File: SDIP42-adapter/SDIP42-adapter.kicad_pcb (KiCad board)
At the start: 2 copper layers, 17.4 x 37.8 mm, 2 parts, among them U1 KM23C32000AG-adaptor, U2 27C322

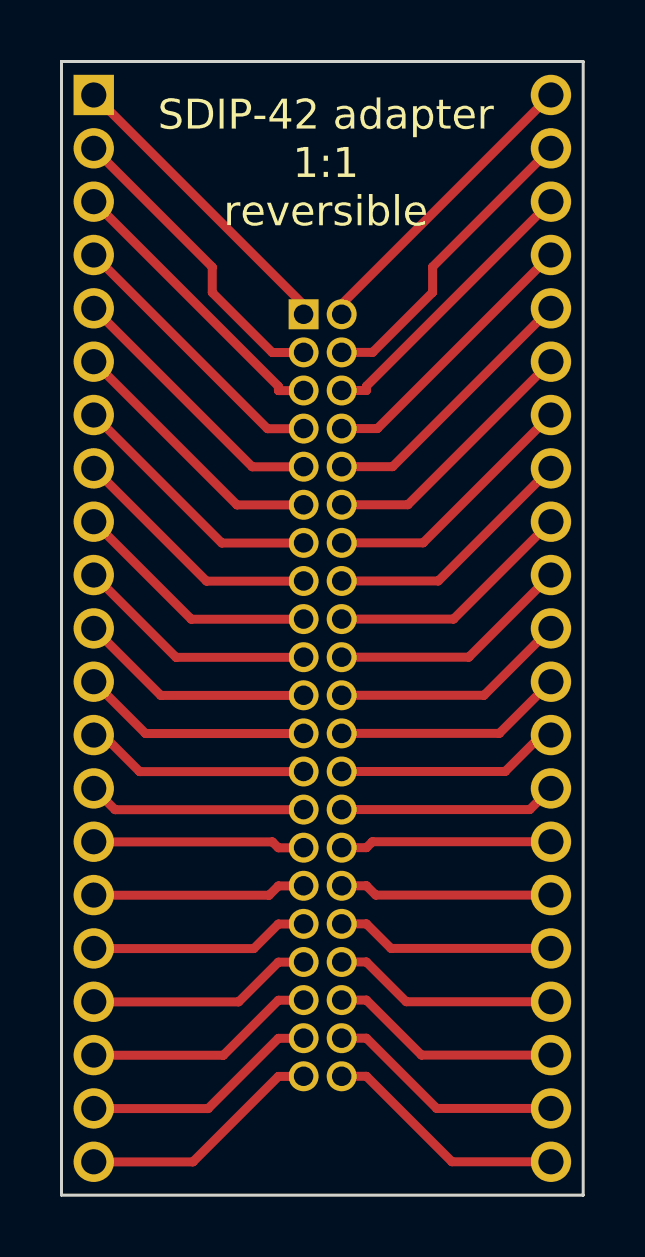
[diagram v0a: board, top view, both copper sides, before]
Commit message: rename projects, update design
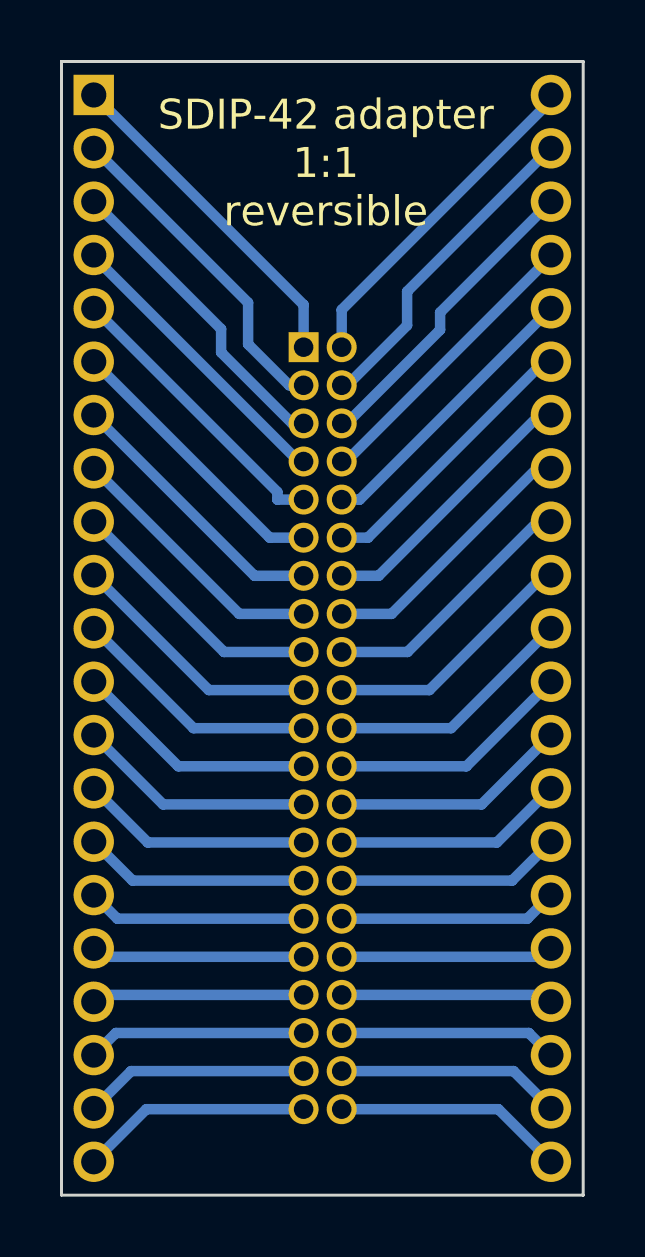
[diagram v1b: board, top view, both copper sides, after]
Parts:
- moved U1 1.10 mm to (145.2, 71.3)
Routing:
- net Net-(U1-Pad1): track 10.2 -> 11.3 mm
- net Net-(U1-Pad42): track 10.2 -> 11.3 mm
- net Net-(U1-Pad3): track 9.67 -> 10.5 mm
- net Net-(U1-Pad2): track 10.3 -> 11.1 mm
- net Net-(U1-Pad40): track 9.67 -> 10.4 mm
- net Net-(U1-Pad5): track 9.16 -> 9.79 mm
- net Net-(U1-Pad41): track 10.3 -> 10.9 mm
- net Net-(U1-Pad4): track 9.37 -> 9.88 mm
